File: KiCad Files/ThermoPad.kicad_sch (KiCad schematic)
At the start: 8 parts, among them J1 Conn_02x01, SW1 SW_Push, U1 XIAO-RP2040-DIP, U2 DM-OLED096-636, U3 SHT30-DIS-B2.5KS

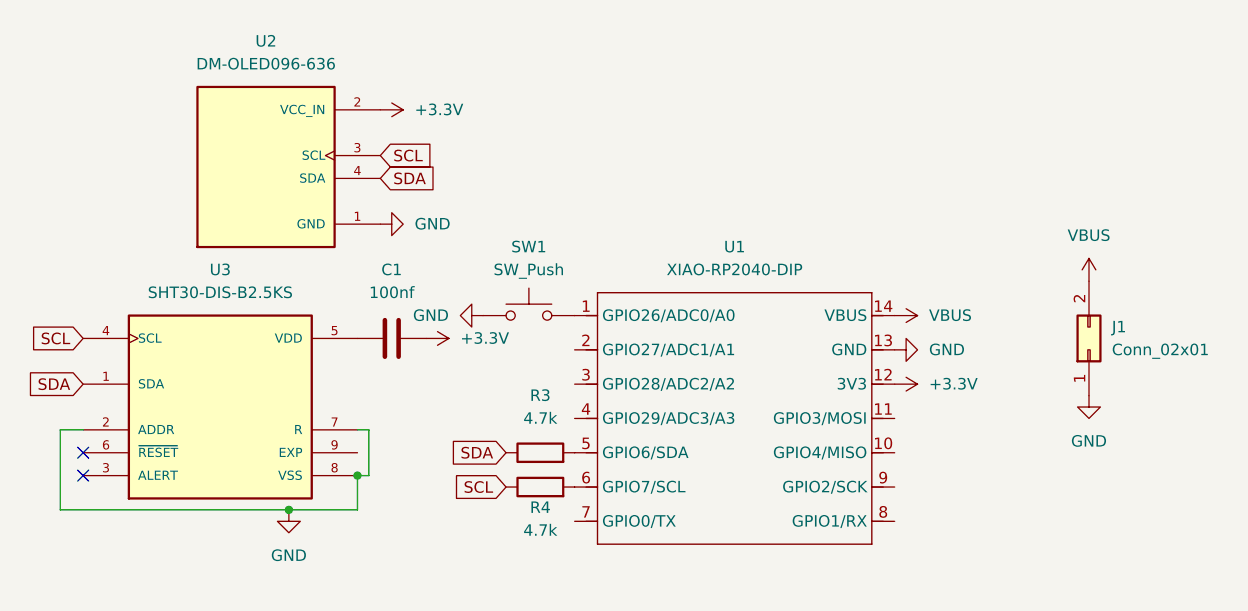
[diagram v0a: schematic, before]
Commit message: Update Pull-Up Resistors
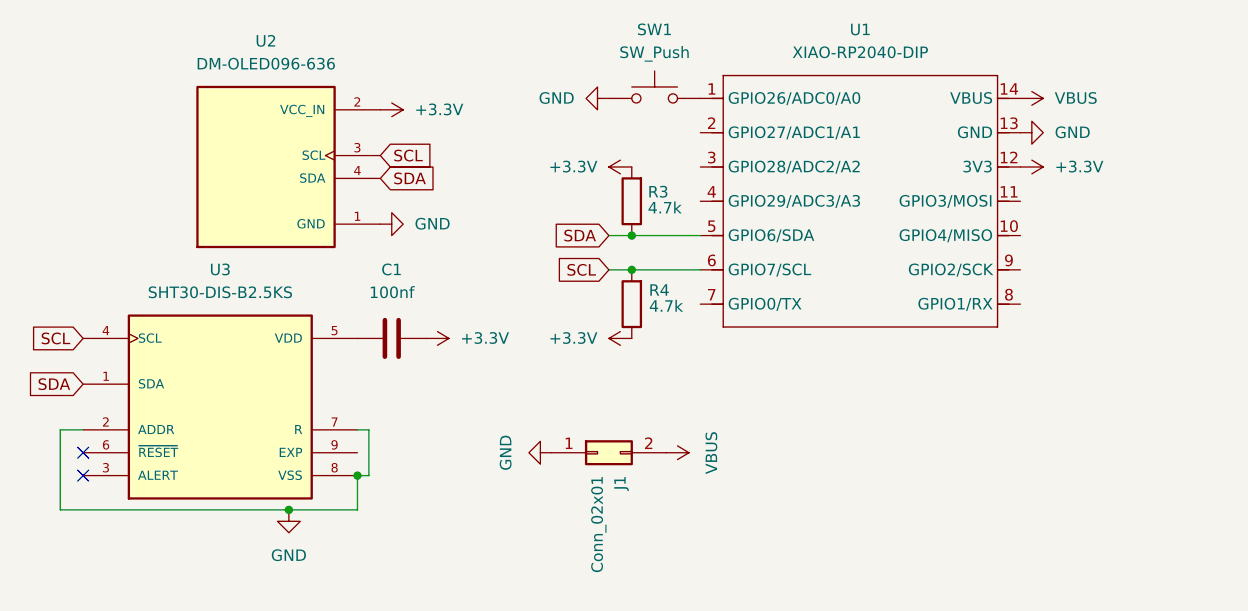
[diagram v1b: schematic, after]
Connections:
- net +3.3V: now also R3.2, R4.1
- net SCL: now also R4.2, U1.6 (GPIO7/SCL); no longer R4.1
- net SDA: now also U1.5 (GPIO6/SDA)
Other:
- moved on the sheet: J1, R3, R4, SW1, U1
